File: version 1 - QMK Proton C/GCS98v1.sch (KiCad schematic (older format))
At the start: 1 part

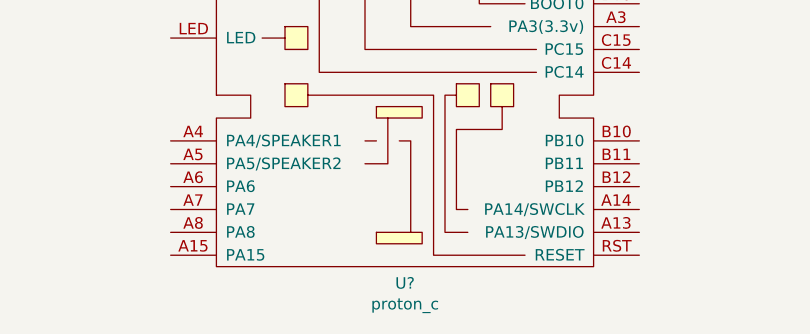
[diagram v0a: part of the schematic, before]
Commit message: footprint assignments
Proton C didn't have a footprint available, will need to create a footprint with pin array
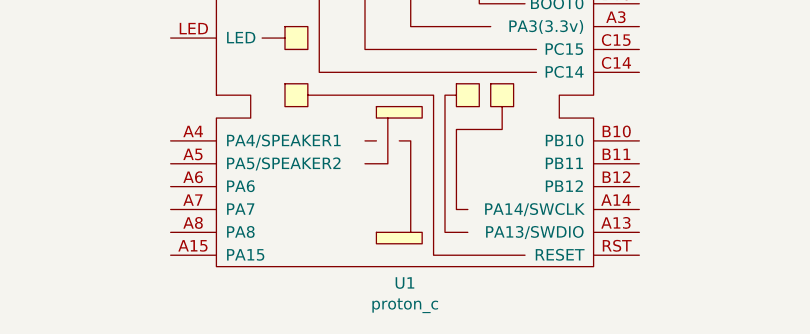
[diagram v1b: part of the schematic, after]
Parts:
- gave numbers to parts that had none: 1
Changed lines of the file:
@@
 $EndDescr
 $Comp
-L proton_c:proton_c U?
+L proton_c:proton_c U1
 U 1 1 60FE4363
 P 5700 4650
-F 0 "U?" H 5675 3127 50  0000 C CNN
+F 0 "U1" H 5675 3127 50  0000 C CNN
 F 1 "proton_c" H 5675 3036 50  0000 C CNN
 F 2 "" H 5550 4650 50  0001 C CNN
@@
 	7050 3750 6700 3750
 $Comp
-L power:GND #PWR?
+L power:GND #PWR0101
 U 1 1 60FEF23D
 P 7050 3750
-F 0 "#PWR?" H 7050 3500 50  0001 C CNN
+F 0 "#PWR0101" H 7050 3500 50  0001 C CNN
 F 1 "GND" H 7055 3577 50  0000 C CNN
 F 2 "" H 7050 3750 50  0001 C CNN
@@
 	6700 3650 6850 3650
 $Comp
-L power:GND #PWR?
+L power:GND #PWR0102
 U 1 1 60FEE0D7
 P 4450 3750
-F 0 "#PWR?" H 4450 3500 50  0001 C CNN
+F 0 "#PWR0102" H 4450 3500 50  0001 C CNN
 F 1 "GND" H 4455 3577 50  0000 C CNN
 F 2 "" H 4450 3750 50  0001 C CNN
@@
 $EndComp
 $Comp
-L power:+5V #PWR?
+L power:+5V #PWR0103
 U 1 1 60FEBD15
 P 6850 3650
-F 0 "#PWR?" H 6850 3500 50  0001 C CNN
+F 0 "#PWR0103" H 6850 3500 50  0001 C CNN
 F 1 "+5V" H 6865 3823 50  0000 C CNN
 F 2 "" H 6850 3650 50  0001 C CNN
